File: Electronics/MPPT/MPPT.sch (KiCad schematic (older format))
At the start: 109 parts, among them J1 Solar Array, J2 Battery, J3 Car Power, J4 CAN_In, J5 CAN_Out, Q1 200N25N, Q2 200N25N, SW1 RESET, SW2 CAN Address, U1 PQMC3-D12-S9-S, U2 Nucleo_L432KC, U3 UCC37321, U4 INA213, U5 ADM3055E, U6 INA213, U7 CDSOT23-T24CAN

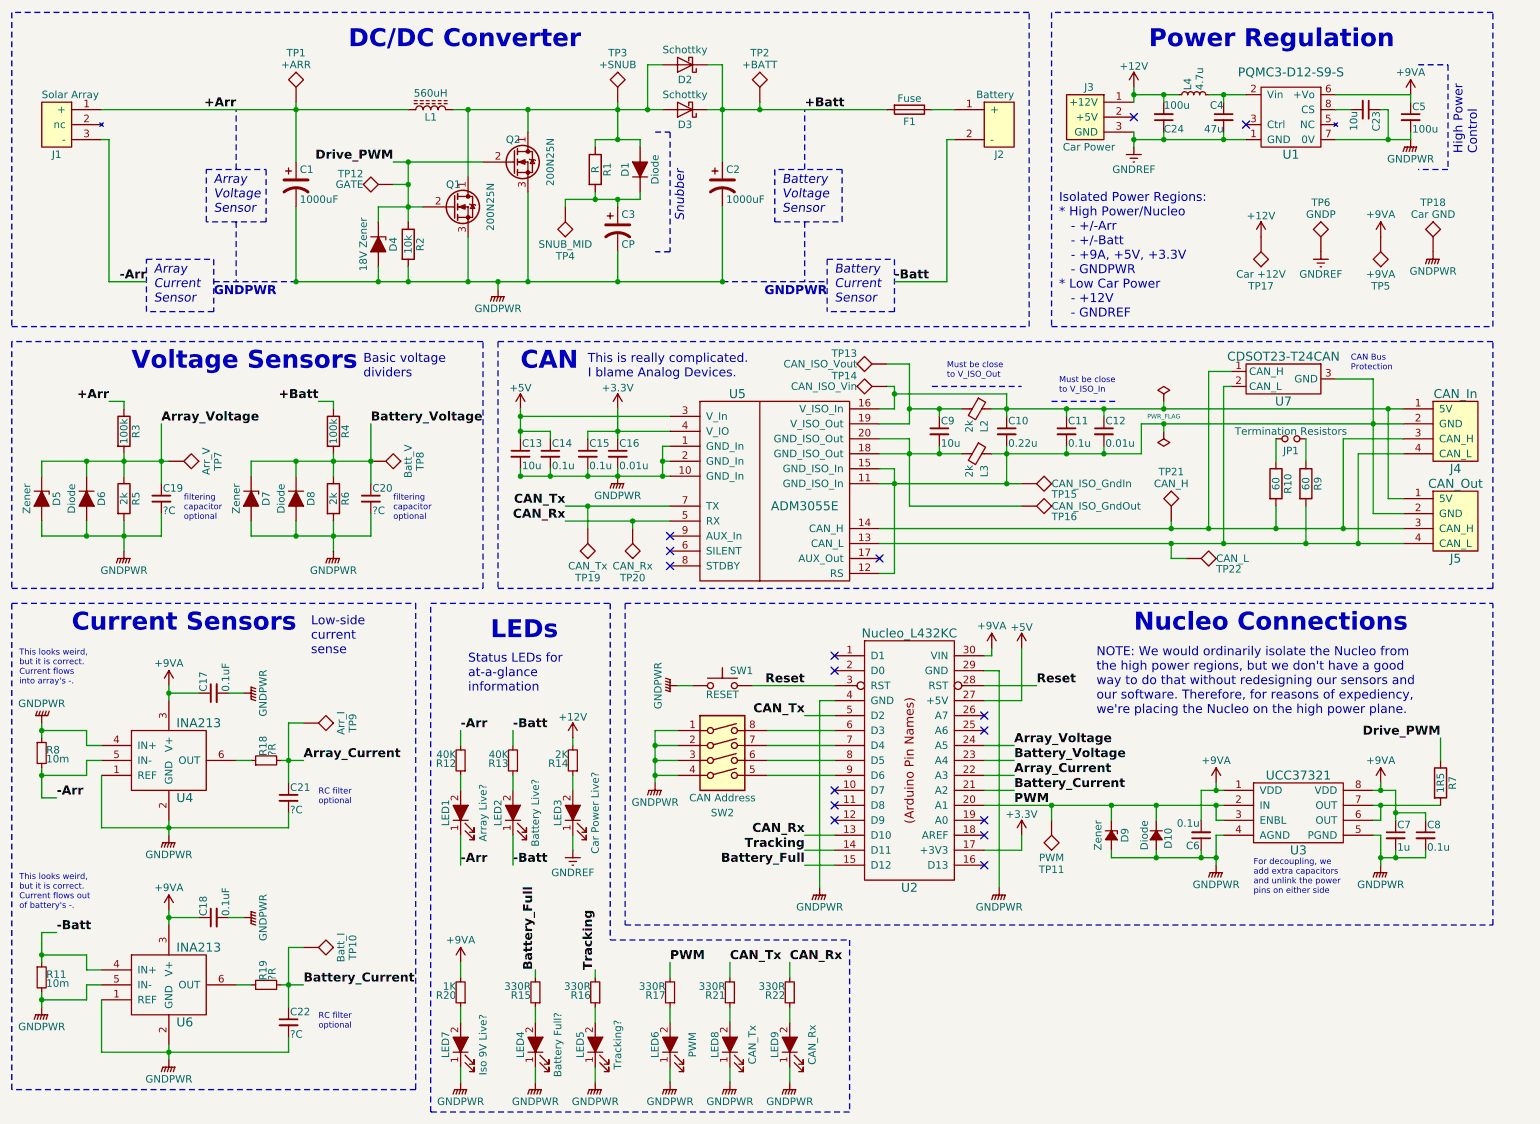
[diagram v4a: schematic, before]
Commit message: MPPT: Fix ground test points for Car Power and Iso. 9V
I had the test points for the grounds of these two voltage levels swapped by mistake. This fixes that error.
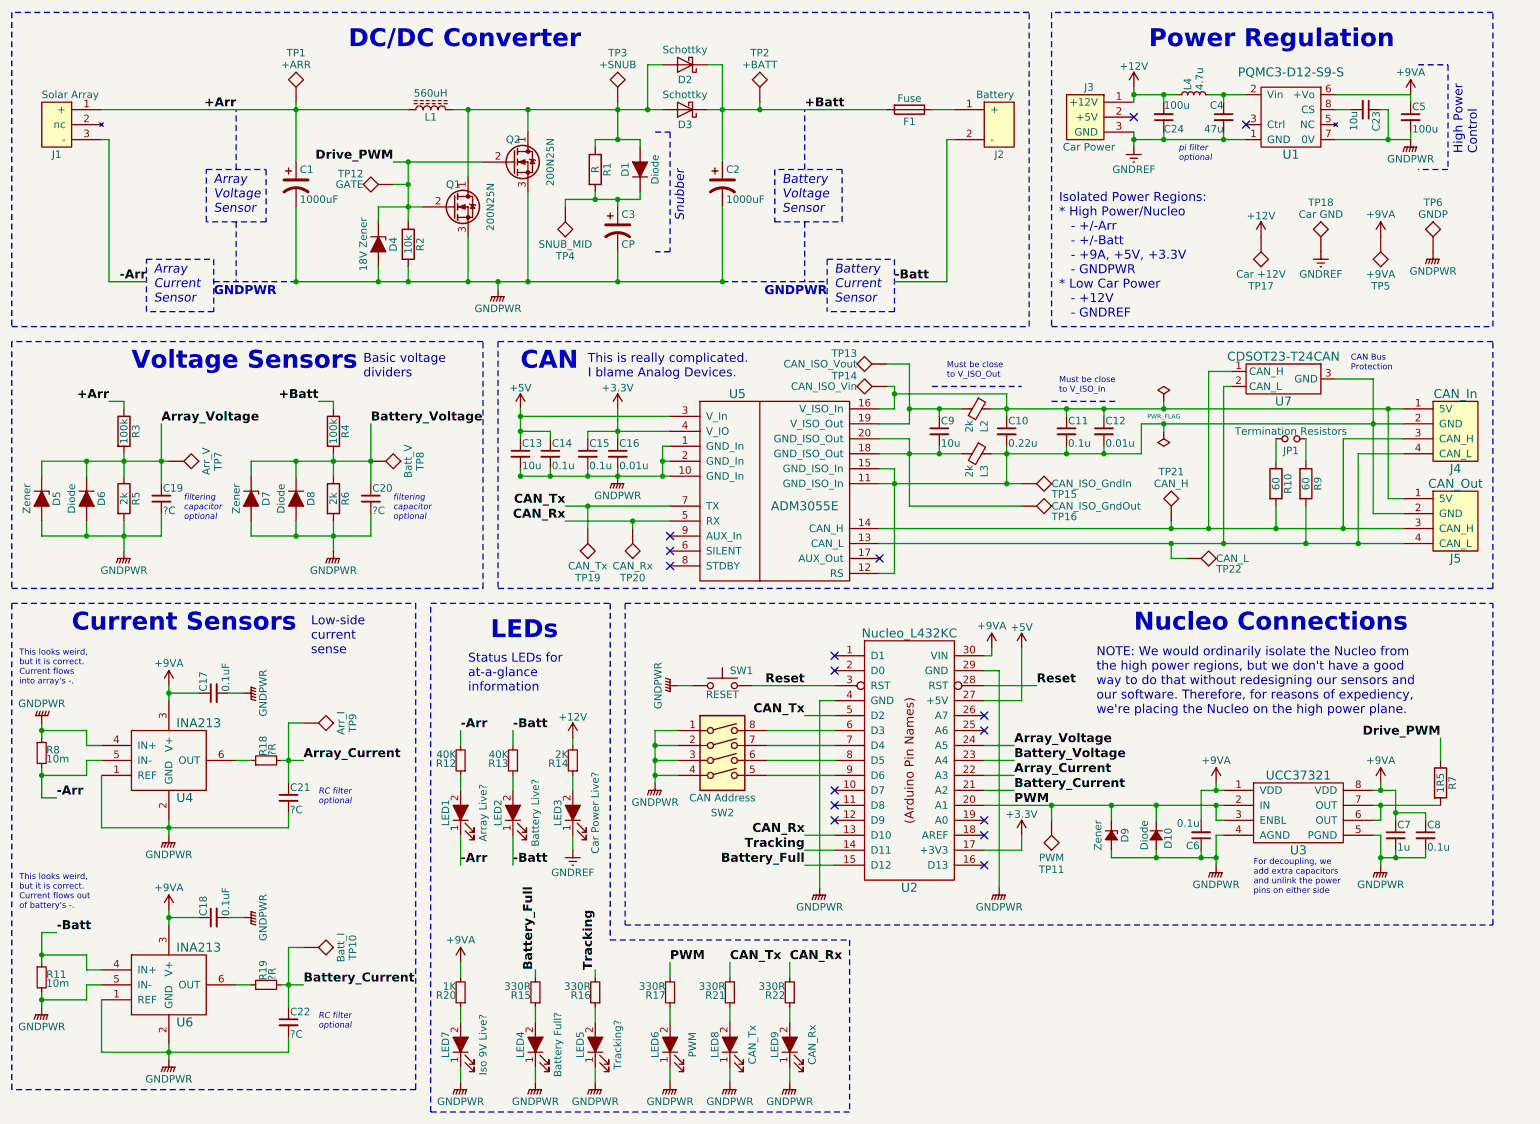
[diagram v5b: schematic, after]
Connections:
- net GNDPWR: now also TP6.1; no longer TP18.1
- net GNDREF: now also TP18.1; no longer TP6.1
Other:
- note added: "pi filter\noptional"
- moved on the sheet: TP18, TP6
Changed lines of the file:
@@
 L TEST TP6
 U 1 1 5BBEBBC8
-P 9300 2150
-F 0 "TP6" H 9300 2450 50  0000 C BNN
-F 1 "GNDP" H 9300 2400 50  0000 C CNN
-F 2 "Measurement_Points:Test_Point_Keystone_5005-5009_Compact" H 9300 2150 50  0001 C CNN
-F 3 "" H 9300 2150 50  0001 C CNN
-	1    9300 2150
+P 10050 2150
+F 0 "TP6" H 10050 2450 50  0000 C BNN
+F 1 "GNDP" H 10050 2400 50  0000 C CNN
+F 2 "Measurement_Points:Test_Point_Keystone_5005-5009_Compact" H 10050 2150 50  0001 C CNN
+F 3 "" H 10050 2150 50  0001 C CNN
+	1    10050 2150
 	1    0    0    -1
 $EndComp
@@
 L TEST TP18
 U 1 1 5BC42C00
-P 10050 2150
-F 0 "TP18" H 10050 2450 50  0000 C BNN
-F 1 "Car GND" H 10050 2400 50  0000 C CNN
-F 2 "Measurement_Points:Test_Point_Keystone_5005-5009_Compact" H 10050 2150 50  0001 C CNN
-F 3 "" H 10050 2150 50  0001 C CNN
-	1    10050 2150
+P 9300 2150
+F 0 "TP18" H 9300 2450 50  0000 C BNN
+F 1 "Car GND" H 9300 2400 50  0000 C CNN
+F 2 "Measurement_Points:Test_Point_Keystone_5005-5009_Compact" H 9300 2150 50  0001 C CNN
+F 3 "" H 9300 2150 50  0001 C CNN
+	1    9300 2150
 	1    0    0    -1
 $EndComp
@@
 	1    0    0    -1
 $EndComp
-Text Notes 3100 3950 0    40   ~ 0
+Text Notes 3100 3950 0    40   Italic 0
 filtering\ncapacitor\noptional
 $Comp
@@
 	1    0    0    -1
 $EndComp
-Text Notes 2600 5850 0    40   ~ 0
+Text Notes 2600 5850 0    40   Italic 0
 RC filter\noptional
 $Comp
@@
 	1    0    0    -1
 $EndComp
-Text Notes 2600 7350 0    40   ~ 0
+Text Notes 2600 7350 0    40   Italic 0
 RC filter\noptional
 $Comp
@@
 	8700 2950 8550 2950
 Wire Wire Line
-	8550 4000 8550 2950
+	8550 2950 8550 4000
 Connection ~ 8550 4000
 Wire Wire Line
-	8650 4100 8650 3050
+	8650 3050 8650 4100
 Connection ~ 8650 4100
 Wire Wire Line
@@
 Wire Wire Line
 	3550 7600 3550 7700
-Text Notes 1700 3950 0    40   ~ 0
+Text Notes 1700 3950 0    40   Italic 0
 filtering\ncapacitor\noptional
 $Comp
@@
 	8300 4200 8400 4200
 Connection ~ 8300 4100
+Text Notes 8350 1550 0    40   Italic 0
+pi filter\noptional
 $EndSCHEMATC

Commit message: MPPT: Fix Array/Battery Live LED circuits; add -Arr and -Batt test points
In the circuits for the Array and Battery Live LEDs, I accidentally had the current flowing through the resistors from - to -, rather than + to -! That was a rather embarrassing mistake.
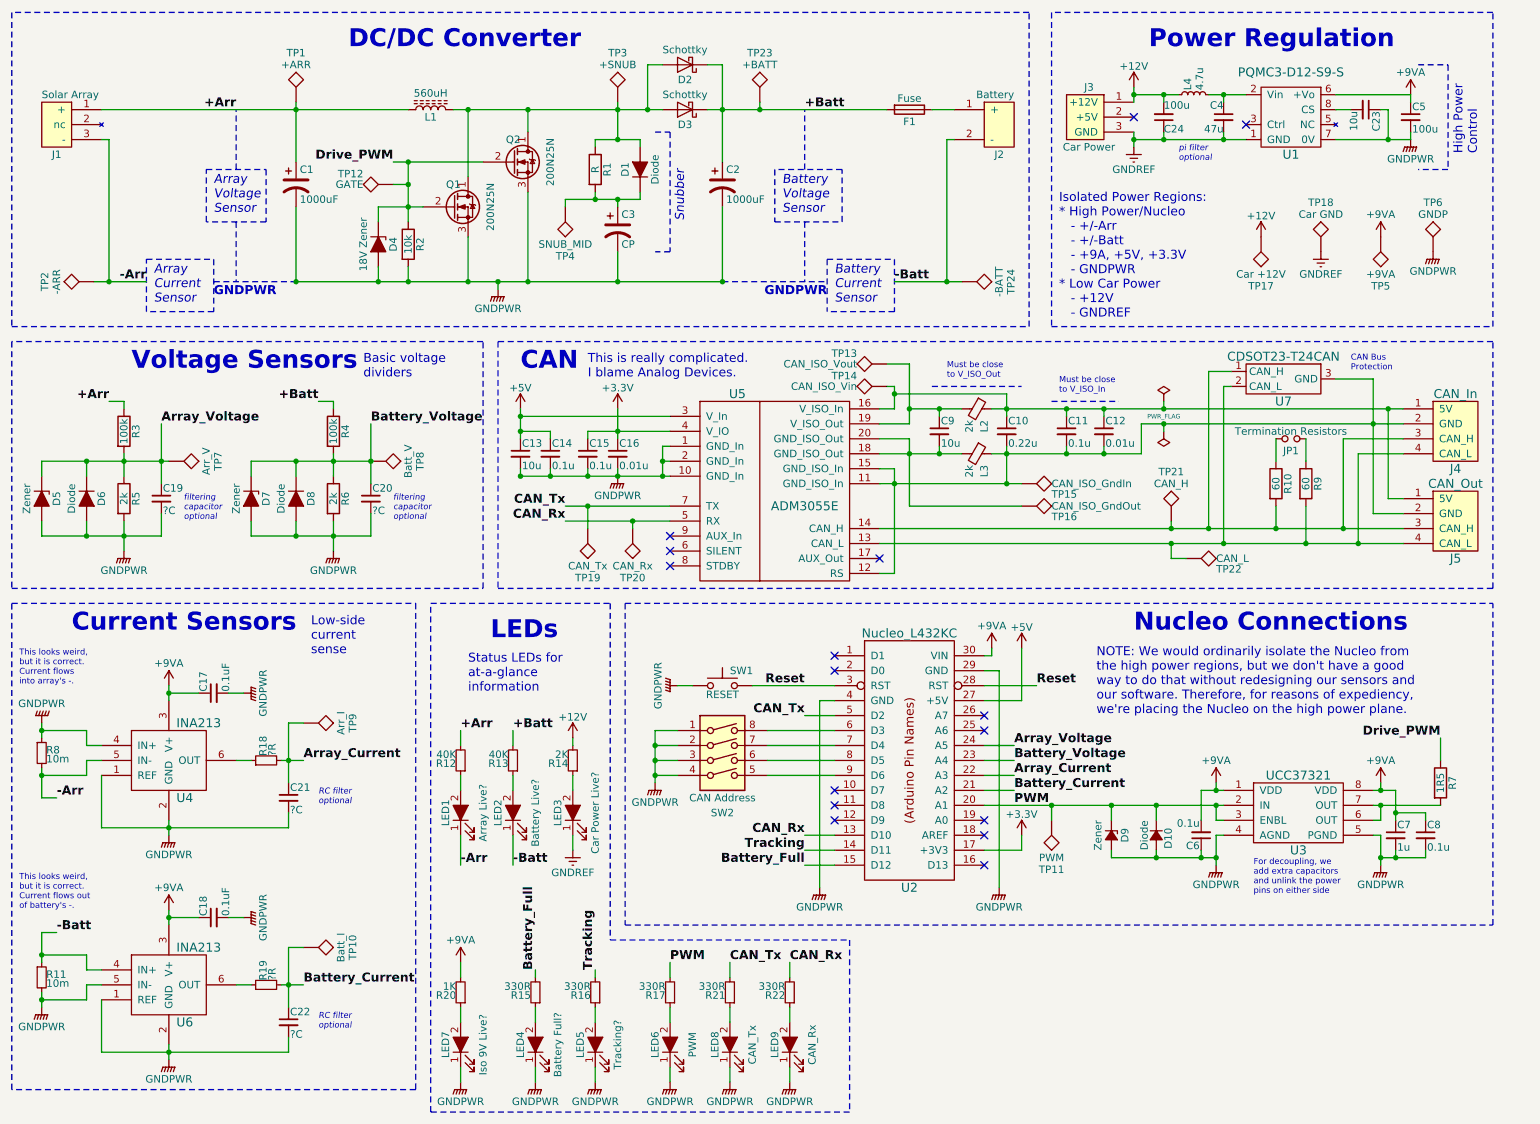
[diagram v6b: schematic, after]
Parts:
- added TP23: +BATT, Measurement_Points:Test_Point_Keystone_5005-5009_Compact, symbol TEST
- added TP24: -BATT, Measurement_Points:Test_Point_Keystone_5005-5009_Compact, symbol TEST
- TP2: value +BATT -> -ARR
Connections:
- net +Arr: now also R12.2
- net +Batt: now also R13.2, TP23.1; no longer TP2.1
- net -Arr: now also TP2.1; no longer R12.2
- net -Batt: now also TP24.1; no longer R13.2
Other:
- moved on the sheet: TP2
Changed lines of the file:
@@
 L TEST TP2
 U 1 1 5BBECCC0
-P 5550 1150
-F 0 "TP2" H 5550 1450 50  0000 C BNN
-F 1 "+BATT" H 5550 1400 50  0000 C CNN
-F 2 "Measurement_Points:Test_Point_Keystone_5005-5009_Compact" H 5550 1150 50  0001 C CNN
-F 3 "" H 5550 1150 50  0001 C CNN
-	1    5550 1150
-	1    0    0    -1
+P 1100 2350
+F 0 "TP2" H 1100 2650 50  0000 C BNN
+F 1 "-ARR" H 1100 2600 50  0000 C CNN
+F 2 "Measurement_Points:Test_Point_Keystone_5005-5009_Compact" H 1100 2350 50  0001 C CNN
+F 3 "" H 1100 2350 50  0001 C CNN
+	1    1100 2350
+	0    -1   -1   0
 $EndComp
 $Comp
@@
 -Arr
 Text Label 3550 5350 0    60   ~ 12
--Arr
++Arr
 Text Label 3900 6250 0    60   ~ 12
 -Batt
 Text Label 3900 5350 0    60   ~ 12
--Batt
++Batt
 $Comp
 L R_Small R15
@@
 	2450 2350 5300 2350
 Wire Wire Line
-	1200 2350 1450 2350
+	1100 2350 1450 2350
 Wire Notes Line
 	1900 2350 2450 2350
@@
 	5300 2350 6000 2350
 Wire Wire Line
-	6800 2350 6450 2350
+	6450 2350 6900 2350
 Wire Wire Line
 	1600 5050 1600 5150
@@
 Text Notes 8350 1550 0    40   Italic 0
 pi filter\noptional
+Connection ~ 1200 2350
+$Comp
+L TEST TP23
+U 1 1 5BCA523D
+P 5550 1150
+F 0 "TP23" H 5550 1450 50  0000 C BNN
+F 1 "+BATT" H 5550 1400 50  0000 C CNN
+F 2 "Measurement_Points:Test_Point_Keystone_5005-5009_Compact" H 5550 1150 50  0001 C CNN
+F 3 "" H 5550 1150 50  0001 C CNN
+	1    5550 1150
+	1    0    0    -1
+$EndComp
+$Comp
+L TEST TP24
+U 1 1 5BCA5488
+P 6900 2350
+F 0 "TP24" H 6900 2650 50  0000 C BNN
+F 1 "-BATT" H 6900 2600 50  0000 C CNN
+F 2 "Measurement_Points:Test_Point_Keystone_5005-5009_Compact" H 6900 2350 50  0001 C CNN
+F 3 "" H 6900 2350 50  0001 C CNN
+	1    6900 2350
+	0    1    1    0
+$EndComp
+Connection ~ 6800 2350
 $EndSCHEMATC

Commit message: MPPT: Several changes to sensors on schematic
Updated current sensor chip and shunt values: INA210 with 2mOhm resistor.

Correct shunt footprint: Was a 2512, not a 2816.

Add resistor to filter on voltage sensors. Filled our RC filter parameters: 1uF cap and 1.7kOhm res.
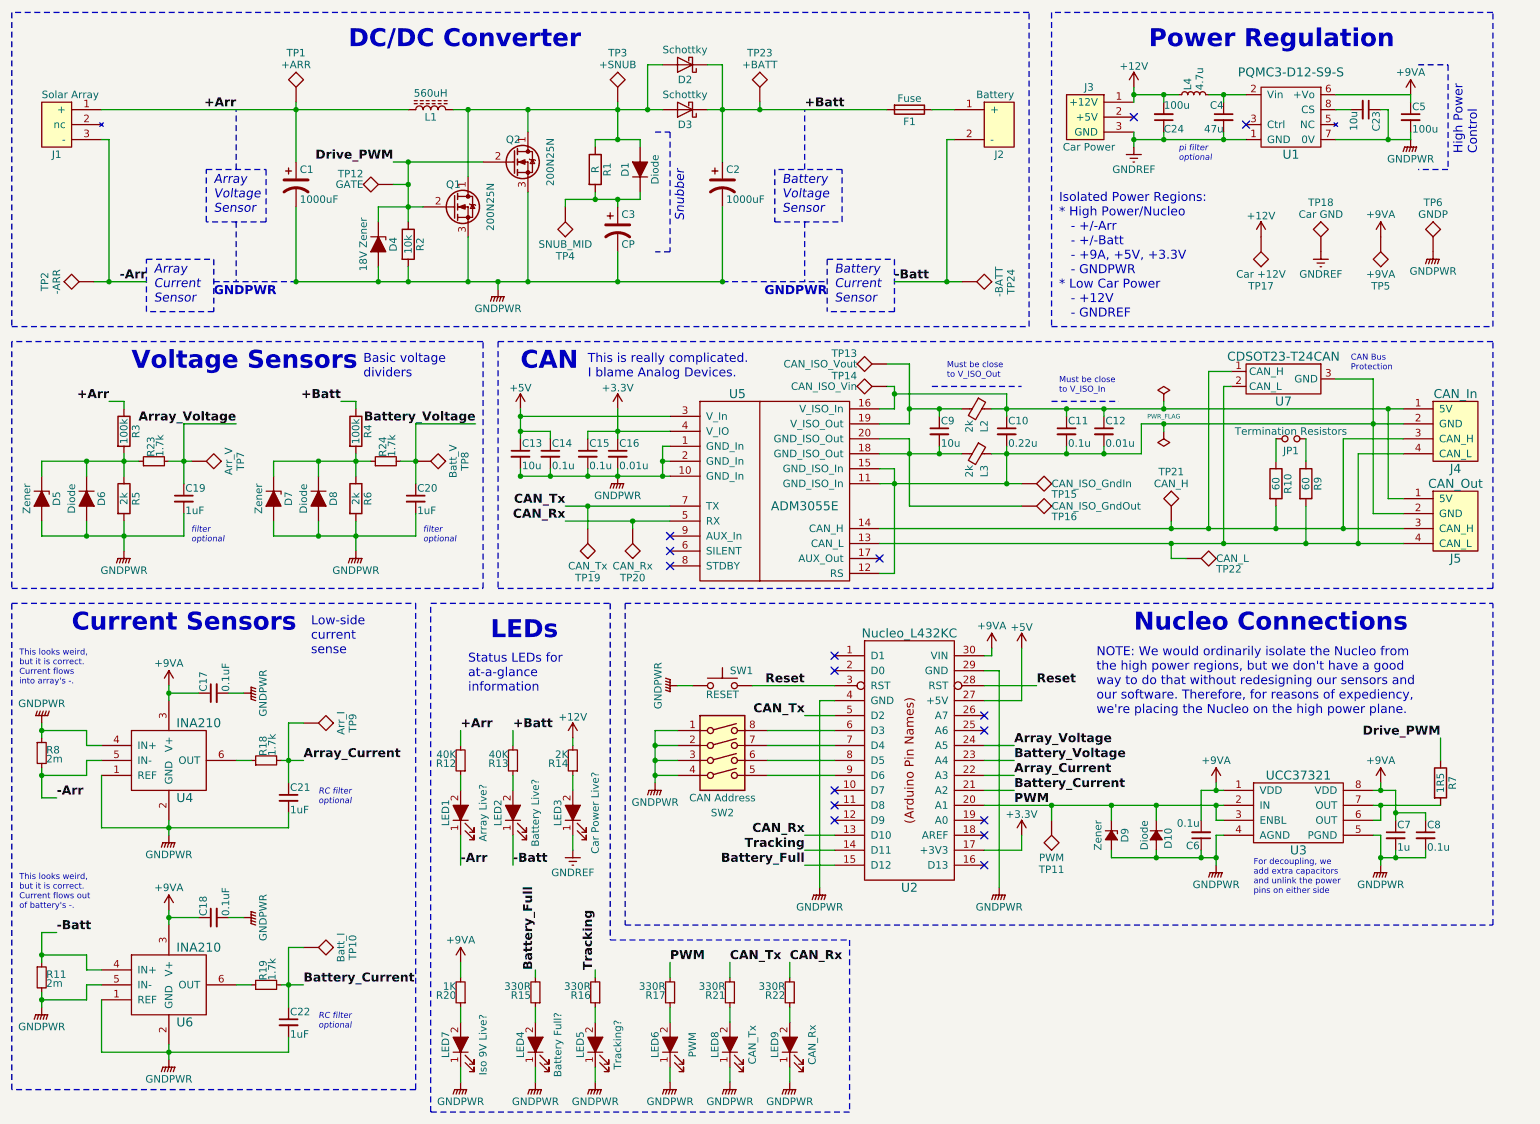
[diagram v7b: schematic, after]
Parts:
- added R23, R24: 1.7k, Resistors_SMD:R_0805_HandSoldering, symbol R_Small
- C19, C20, C21, C22: value ?C -> 1uF
- R11, R8: value 10m -> 2m; footprint Resistors_SMD:R_2816_HandSoldering -> Resistors_SMD:R_2512_HandSoldering
- R18, R19: value ?R -> 1.7k
- U4, U6: value INA213 -> INA210
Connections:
- net Array_Voltage: now also R23.2; no longer D5.1 (K), D6.1 (K), R3.2, R5.1
- net Battery_Voltage: now also R24.2; no longer D7.1 (K), D8.1 (K), R4.2, R6.1
- new net: D5.1 (K), D6.1 (K), R23.1, R3.2, R5.1
- new net: D7.1 (K), D8.1 (K), R24.1, R4.2, R6.1
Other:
- note added: "filter\noptional"
- note removed: "filtering\ncapacitor\noptional"
- moved on the sheet: C19, C20, D7, D8, R4, R6, TP7, TP8
